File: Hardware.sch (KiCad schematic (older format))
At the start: 25 parts, among them J1 Power, J10 Conn_Extra_RJ45, J11 RJ45-Dual, J2 RJ45-Dual, J3 SWD_Conn, J4 Conn_02x04, J5 Spare_Conn, J6 Power_Conn, U1 STM32F042G6Ux, U2 MCP9700T-ETT, U3 MCP9700T-ETT, Y1 8MHz

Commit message: Associated the RP-Diode
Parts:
- D3: footprint (none) -> Diode_SMD:D_SMA_Handsoldering; symbol Device:D_Small -> Device:D_Schottky_Small; Buy (none) -> https://www.digikey.com/product-detail/en/smc-diode-solutio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
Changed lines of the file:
@@
 	850  1700 850  1750
 $Comp
-L Device:D_Small D3
+L Device:D_Schottky_Small D3
 U 1 1 5AE82317
 P 1375 4100
 F 0 "D3" H 1375 4000 50  0000 C CNN
 F 1 "D_Small" H 1375 4200 50  0000 C CNN
-F 2 "" V 1375 4100 50  0001 C CNN
+F 2 "Diode_SMD:D_SMA_Handsoldering" V 1375 4100 50  0001 C CNN
 F 3 "~" V 1375 4100 50  0001 C CNN
+F 4 "https://www.digikey.com/product-detail/en/smc-diode-solutions/15MQ060NTR/1655-1353-1-ND/6022798" H 1375 4100 50  0001 C CNN "Buy"
 	1    1375 4100
 	-1   0    0    1

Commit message: Associated the ESP_Conn
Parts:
- J4: value Conn_02x04 -> ESP_Conn; footprint (none) -> Connector_PinHeader_2.54mm:PinHeader_2x04_P2.54mm_Vertical
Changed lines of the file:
@@
 P 2975 4950
 F 0 "J4" H 3025 4650 50  0000 C CNN
-F 1 "Conn_02x04" H 3025 5176 50  0000 C CNN
-F 2 "" H 2975 4950 50  0001 C CNN
+F 1 "ESP_Conn" H 3025 5176 50  0000 C CNN
+F 2 "Connector_PinHeader_2.54mm:PinHeader_2x04_P2.54mm_Vertical" H 2975 4950 50  0001 C CNN
 F 3 "~" H 2975 4950 50  0001 C CNN
 F 4 "-" H 2975 4950 50  0001 C CNN "Buy"

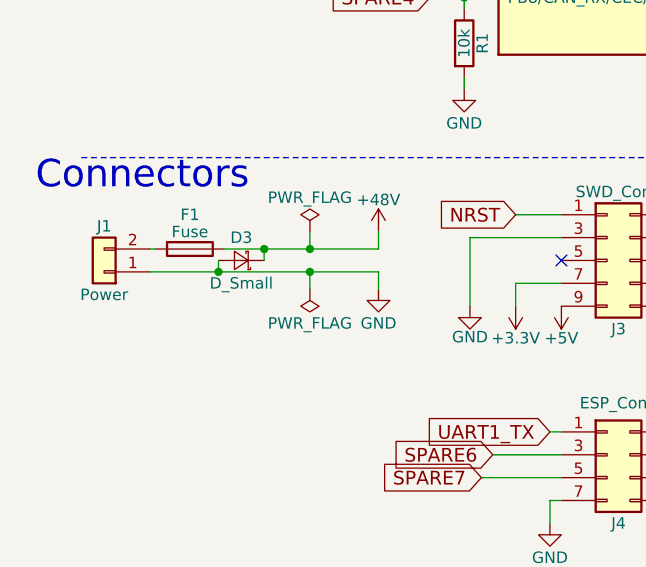
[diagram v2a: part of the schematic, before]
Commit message: Renamed D_Small to D_Schot
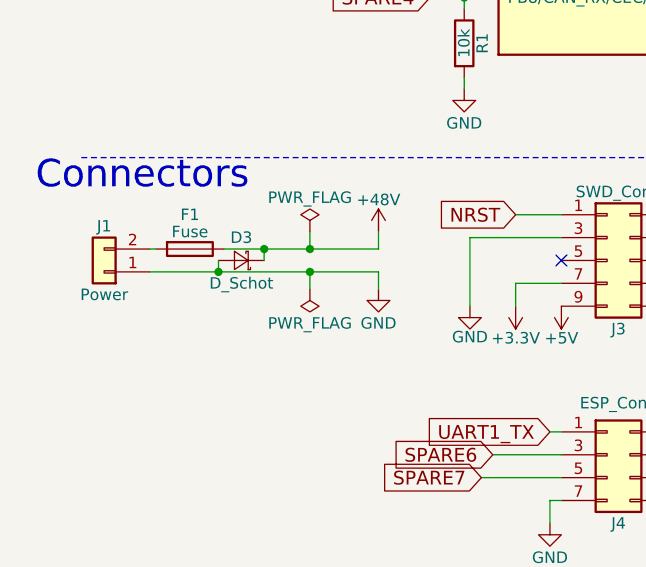
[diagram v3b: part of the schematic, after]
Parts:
- D3: value D_Small -> D_Schot
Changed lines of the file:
@@
 P 1375 4100
 F 0 "D3" H 1375 4000 50  0000 C CNN
-F 1 "D_Small" H 1375 4200 50  0000 C CNN
+F 1 "D_Schot" H 1375 4200 50  0000 C CNN
 F 2 "Diode_SMD:D_SMA_Handsoldering" V 1375 4100 50  0001 C CNN
 F 3 "~" V 1375 4100 50  0001 C CNN

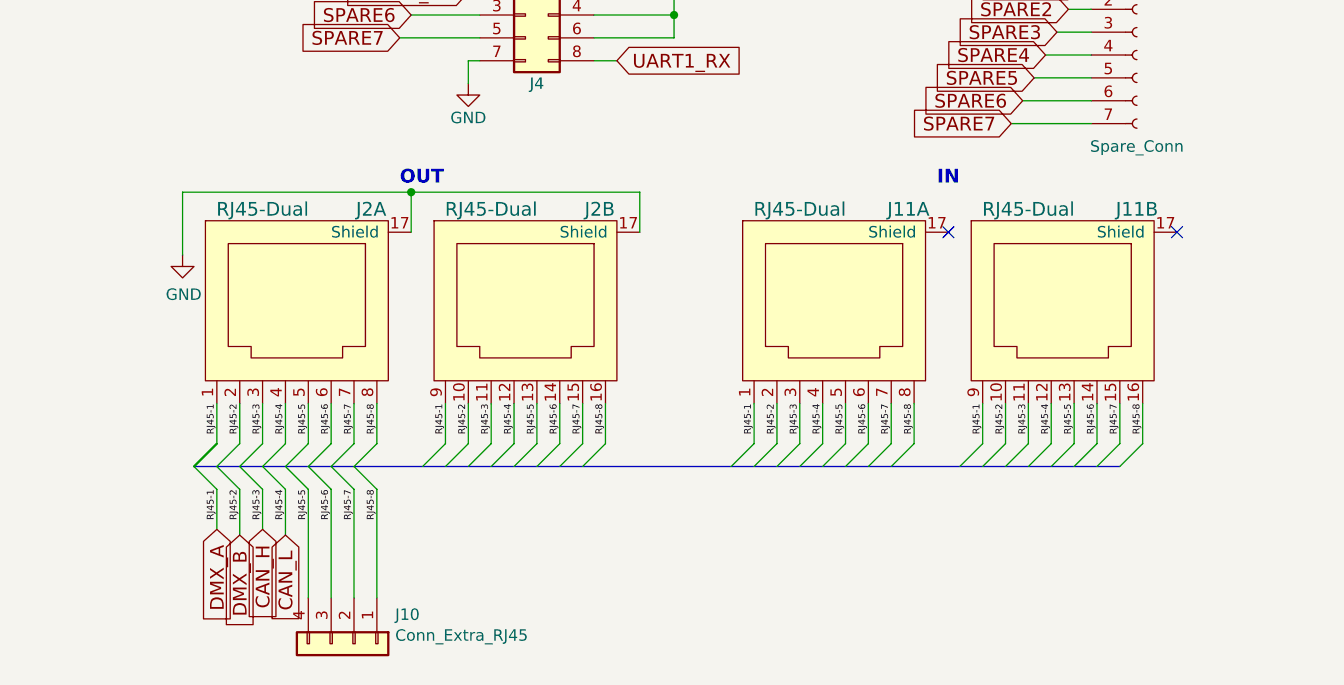
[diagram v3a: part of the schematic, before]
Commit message: Replaced the IN-Connector with the Shieldless-Version
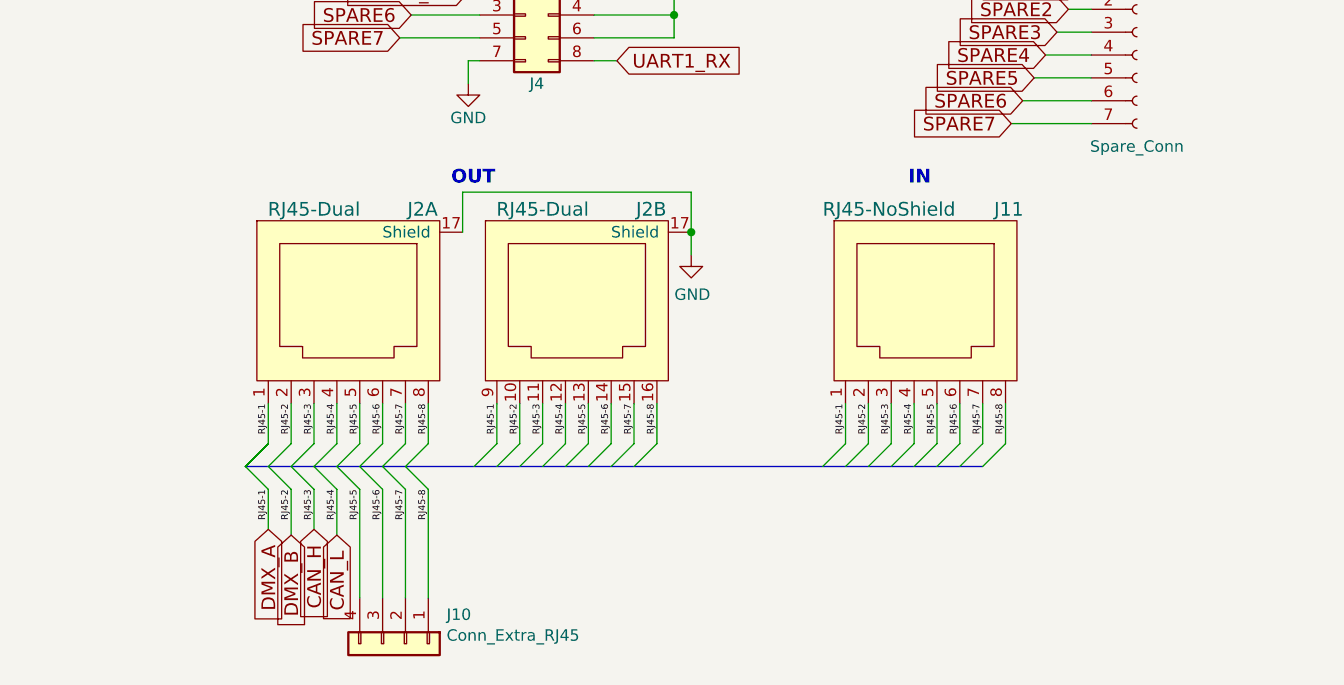
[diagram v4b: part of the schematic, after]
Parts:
- removed J11: RJ45-Dual, symbol connectors:RJ45-Dual
- added J11: RJ45-NoShield, symbol connectors:RJ45-NoShield
- J2: Buy (none) -> -
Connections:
- net CAN_H: now also J11.3
- net CAN_L: now also J11.4
- net DMX_A: now also J11.1
- net DMX_B: now also J11.2
- net RJ45-5: now also J11.5
- net RJ45-6: now also J11.6
- net RJ45-7: now also J11.7
- net RJ45-8: now also J11.8
- no-connect marks 3 -> 1
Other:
- moved on the sheet: J10, J2A, J2B

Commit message: Associated the RJ45-Footprints
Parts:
- J11: footprint (none) -> RJ45:RJ45_NoShield
- J2: footprint (none) -> RJ45:RJ45-Dual
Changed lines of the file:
@@
 F 0 "J2" H 2525 6600 60  0000 C CNN
 F 1 "RJ45-Dual" H 2050 6600 60  0000 C CNN
-F 2 "" H 2150 6150 60  0001 C CNN
+F 2 "RJ45:RJ45-Dual" H 2150 6150 60  0001 C CNN
 F 3 "" H 2150 6150 60  0001 C CNN
 F 4 "-" H 2200 6200 50  0001 C CNN "Buy"
@@
 F 0 "J2" H 3525 6600 60  0000 C CNN
 F 1 "RJ45-Dual" H 3050 6600 60  0000 C CNN
-F 2 "" H 3150 6150 60  0001 C CNN
+F 2 "RJ45:RJ45-Dual" H 3150 6150 60  0001 C CNN
 F 3 "" H 3150 6150 60  0001 C CNN
 F 4 "-" H 3200 6200 50  0001 C CNN "Buy"
@@
 F 0 "J11" H 5025 6600 60  0000 L CNN
 F 1 "RJ45-NoShield" H 4275 6600 60  0000 L CNN
-F 2 "" H 4675 6150 60  0001 C CNN
+F 2 "RJ45:RJ45_NoShield" H 4675 6150 60  0001 C CNN
 F 3 "" H 4675 6150 60  0001 C CNN
 F 4 "-" H 4725 6200 50  0001 C CNN "Buy"

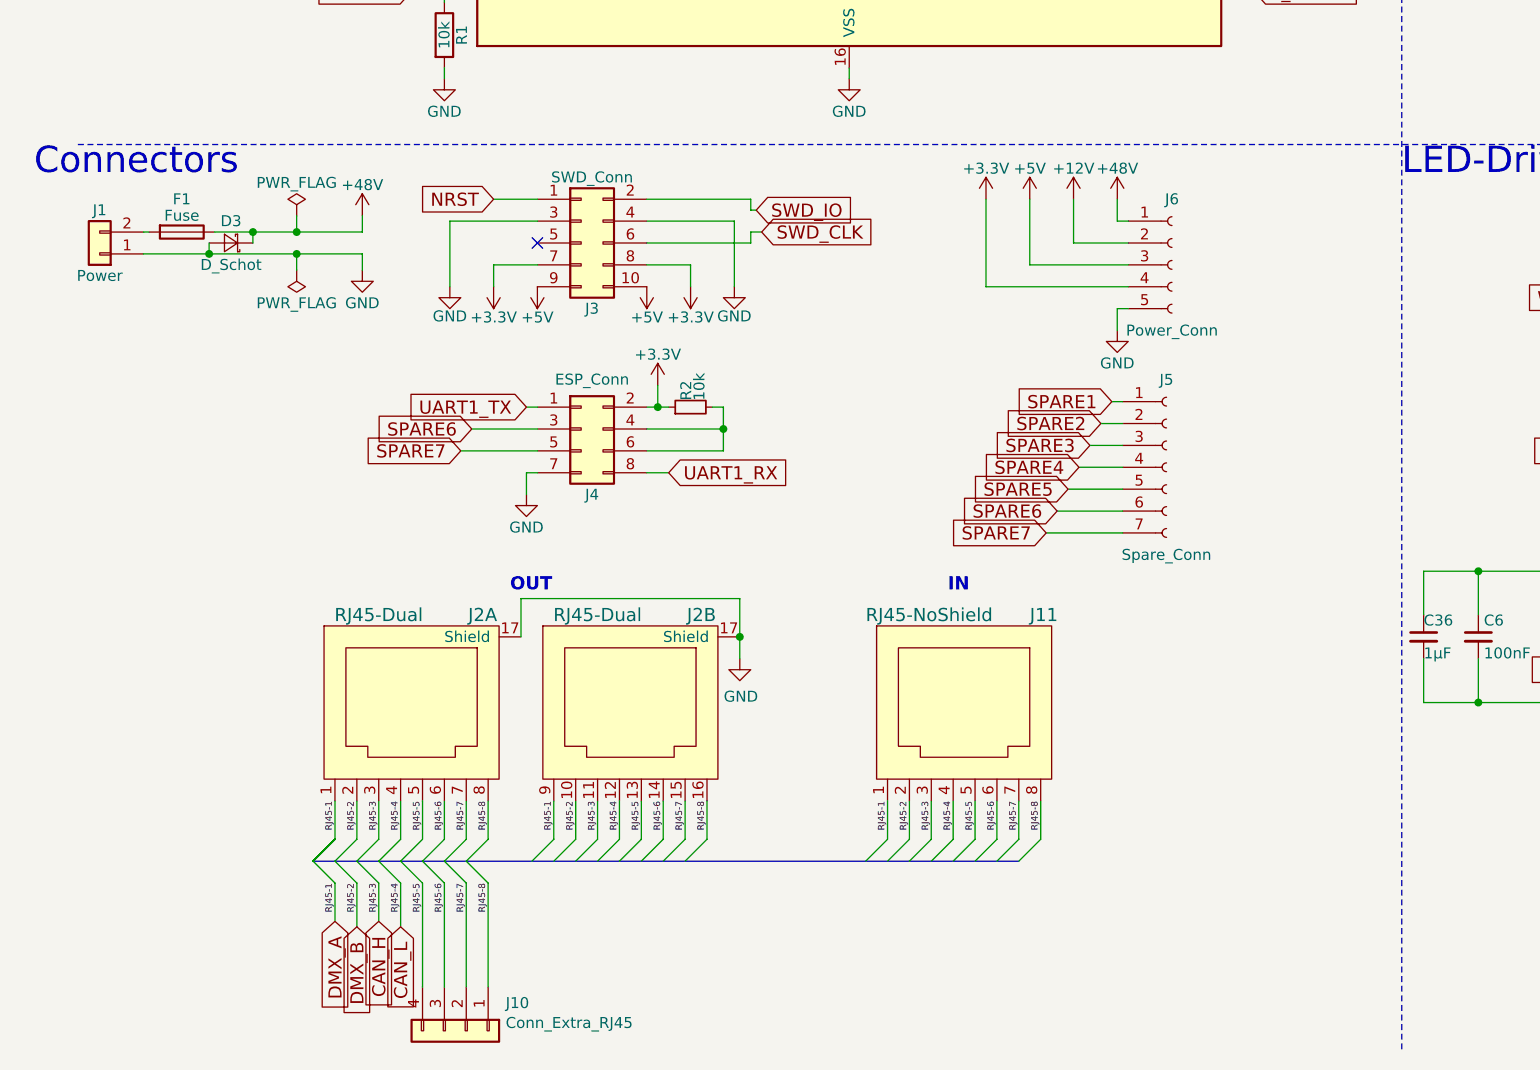
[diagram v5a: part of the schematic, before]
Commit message: Changed RJ45-Mapping to be (semi-)DMX512-compatible
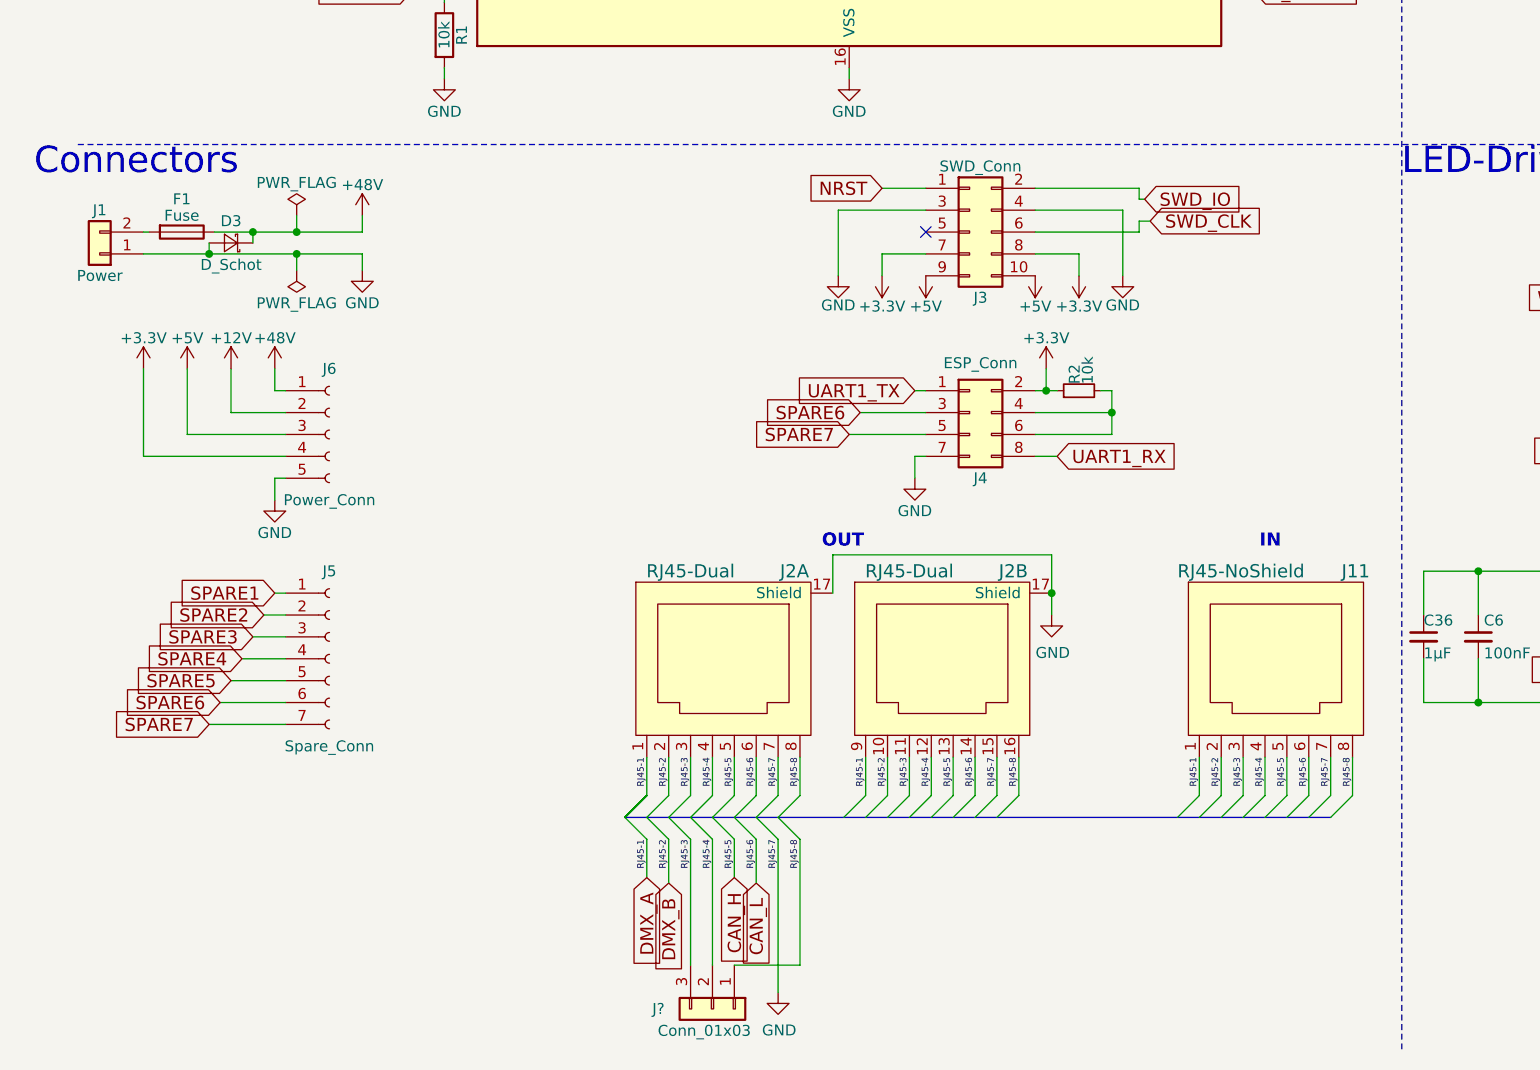
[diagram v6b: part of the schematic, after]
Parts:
- removed J10: Conn_Extra_RJ45, Connector_PinHeader_2.54mm:PinHeader_1x04_P2.54mm_Vertical, symbol Connector_Generic:Conn_01x04
- added J?: Conn_01x03, symbol Connector_Generic:Conn_01x03
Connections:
- net RJ45-5 is gone; now on net CAN_H: J11.5, J2.13, J2.5
- net RJ45-6 is gone; now on net CAN_L: J11.6, J2.14, J2.6
- net RJ45-7 is gone; now on net GND: J11.7, J2.15, J2.7
- net CAN_H: no longer J11.3, J2.11, J2.3
- net CAN_L: no longer J11.4, J2.12, J2.4
- net RJ45-8: now also J?.1 (Pin_1)
- new net RJ45-3: J11.3, J2.11, J2.3, J?.3 (Pin_3)
- new net RJ45-4: J11.4, J2.12, J2.4, J?.2 (Pin_2)
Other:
- moved on the sheet: J11, J2A, J2B, J3, J4, J5, J6, R2
